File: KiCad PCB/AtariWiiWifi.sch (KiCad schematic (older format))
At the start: 16 parts, among them J1 DB9_Male, J1A1 Conn_01x09, J2 DB9_Male, J2A1 Conn_01x09, U1 PCAL6416APW, U2 AD5242, U3 AD5242, U4 ESP32

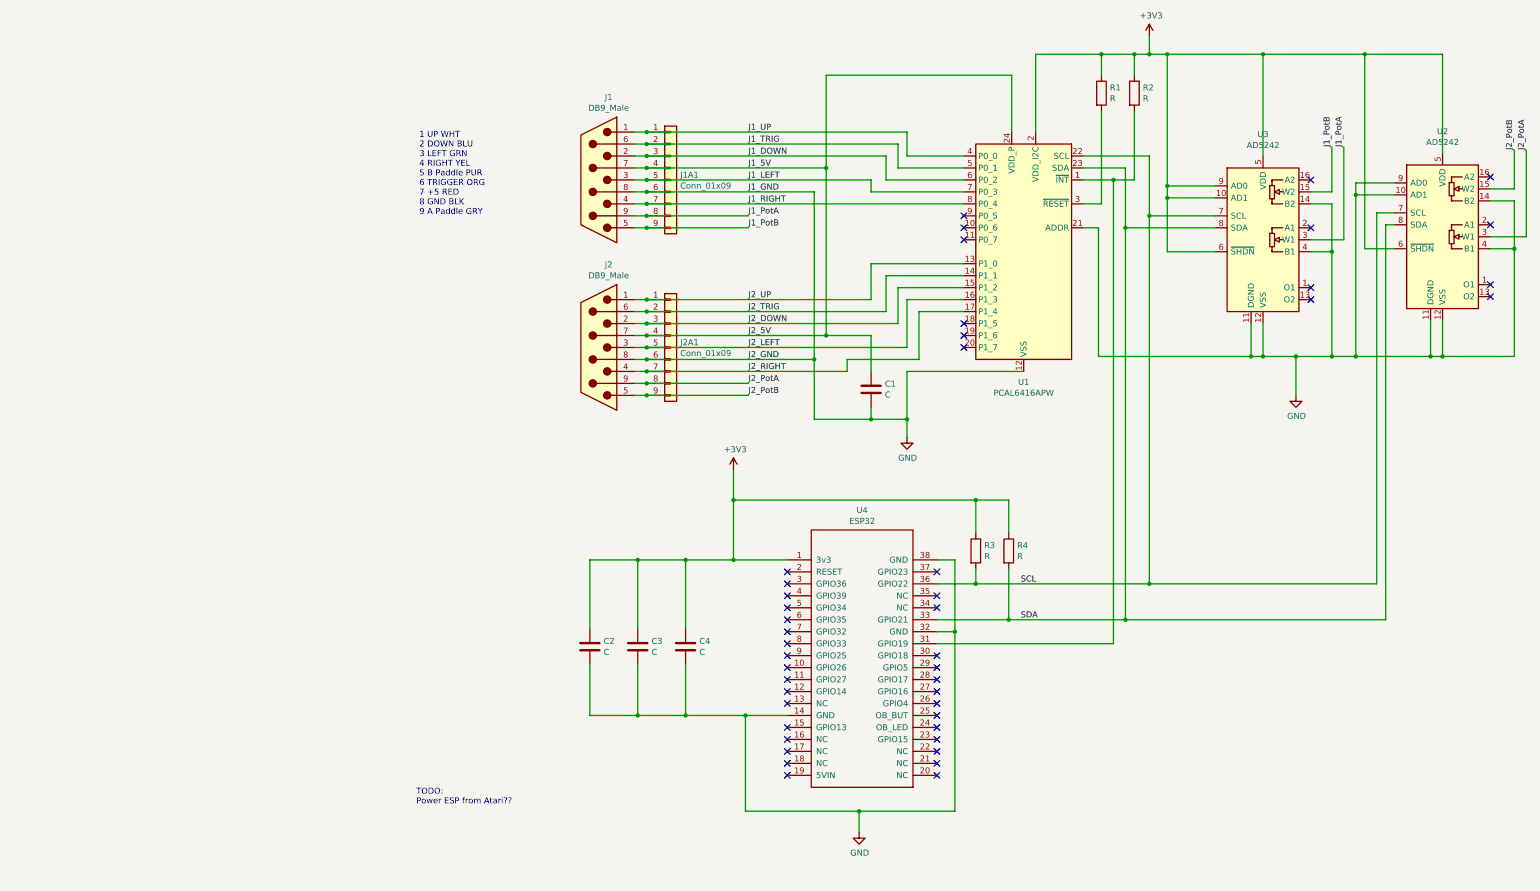
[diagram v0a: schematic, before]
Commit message: Update PCB to Rev 2
Fixed Digital pots connected to ground instead of +5.

Added jumper to power ESP from Atari
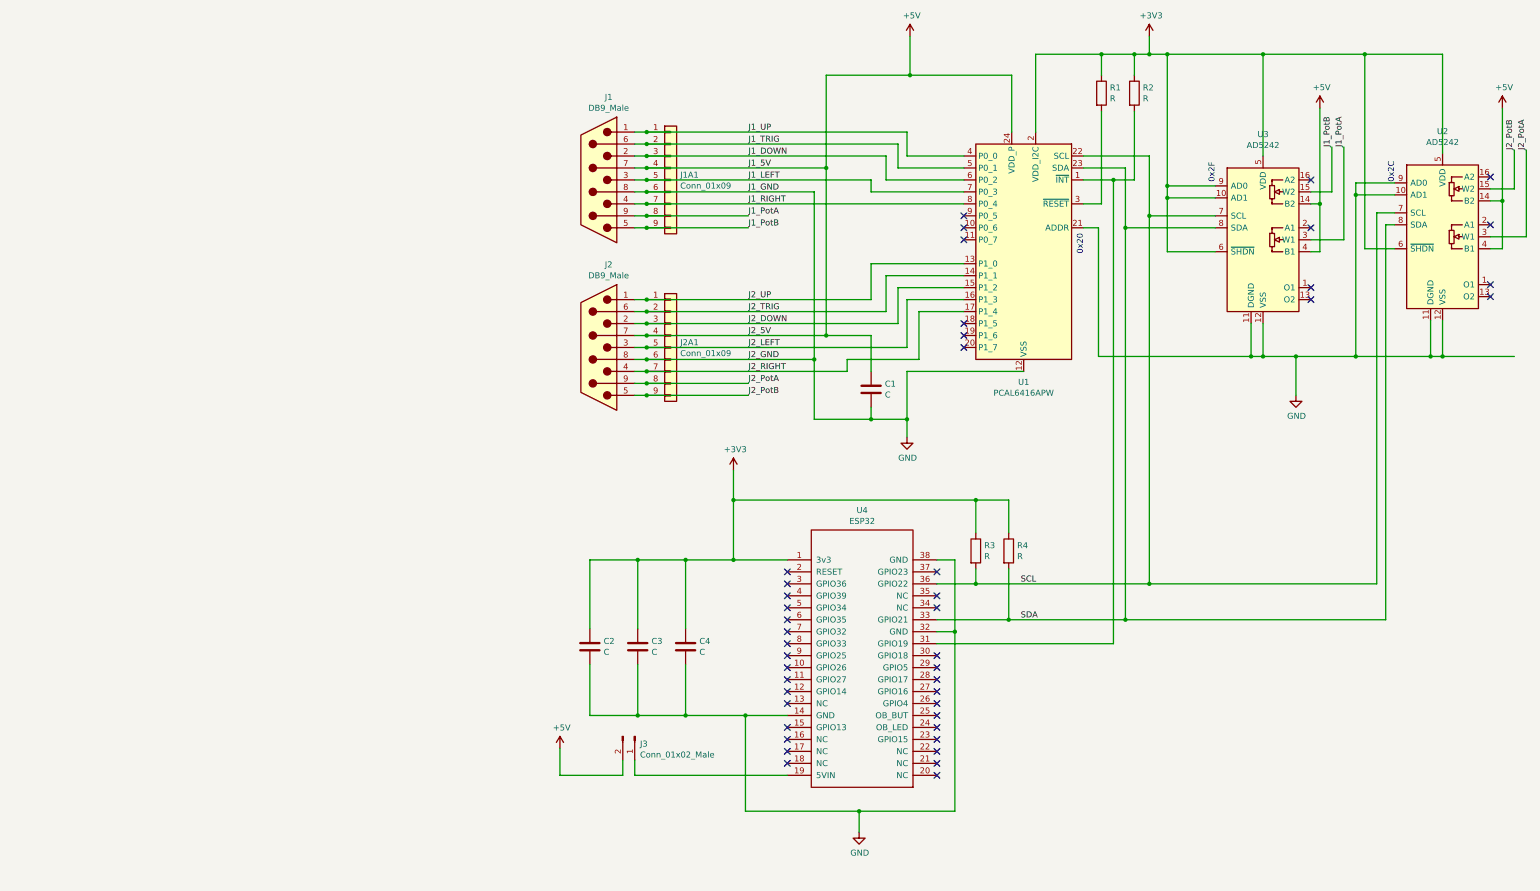
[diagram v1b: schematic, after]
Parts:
- added J3: Conn_01x02_Male, Pin_Headers:Pin_Header_Straight_1x02_Pitch2.54mm, symbol Connector:Conn_01x02_Male
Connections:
- net GND: no longer U2.14 (B2), U2.4 (B1), U3.14 (B2), U3.4 (B1)
- net at U4.19 (5VIN): now also J3.1 (Pin_1)
- net J1_5V renamed +5V
- net +5V: now also U2.14 (B2), U2.4 (B1), U3.14 (B2), U3.4 (B1), J3.2 (Pin_2)
- no-connect marks 45 -> 44
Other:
- note added: "0x20"
- note added: "0x2C"
- note added: "0x2F"
- note removed: "1 UP WHT\n2 DOWN BLU\n3 LEFT GRN\n4 RIGHT YEL\n5 B Paddle PUR\n6 TRIGGER ORG\n7 +5 RED\n8 GND BLK\n9 A Paddle GRY"
- note removed: "TODO:\nPower ESP from Atari??"
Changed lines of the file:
@@
 encoding utf-8
 Sheet 1 1
-Title ""
-Date ""
-Rev ""
-Comp ""
+Title "Atari Wii ESP32 Interfae"
+Date "5/15/21"
+Rev "2"
+Comp "mulcmu"
 Comment1 ""
 Comment2 ""
@@
 	-1   0    0    1
 $EndComp
-Text Notes 1100 2300 0    50   ~ 0
-1 UP WHT\n2 DOWN BLU\n3 LEFT GRN\n4 RIGHT YEL\n5 B Paddle PUR\n6 TRIGGER ORG\n7 +5 RED\n8 GND BLK\n9 A Paddle GRY
 $Comp
 L Connector_Generic:Conn_01x09 J1A1
@@
 $EndComp
 Wire Wire Line
-	4500 1125 6050 1125
+	4500 1125 5200 1125
 Wire Wire Line
 	6050 1125 6050 1600
@@
 Connection ~ 9550 3475
 Wire Wire Line
-	8550 2600 8725 2600
-Wire Wire Line
-	8725 2600 8725 3475
-Connection ~ 8725 3475
-Wire Wire Line
-	8725 3475 8925 3475
-Wire Wire Line
-	8550 2200 8725 2200
-Wire Wire Line
-	8725 2200 8725 2600
-Connection ~ 8725 2600
-Wire Wire Line
-	10050 2575 10250 2575
-Wire Wire Line
-	10250 2575 10250 3475
+	8550 2600 8625 2600
+Wire Wire Line
+	8550 2200 8625 2200
+Wire Wire Line
+	8625 2200 8625 2600
+Wire Wire Line
+	10050 2575 10150 2575
 Wire Wire Line
 	10250 3475 9650 3475
 Connection ~ 9650 3475
 Wire Wire Line
-	10050 2175 10250 2175
-Wire Wire Line
-	10250 2175 10250 2575
-Connection ~ 10250 2575
+	10050 2175 10150 2175
+Wire Wire Line
+	10150 2175 10150 2575
 Text Label 8725 1725 1    50   ~ 0
 J1_PotB
@@
 NoConn ~ 4175 6775
 NoConn ~ 4175 6875
-NoConn ~ 4175 6975
 NoConn ~ 5425 6975
 NoConn ~ 5425 6875
@@
 Connection ~ 8425 3475
 Wire Wire Line
-	8425 3475 8725 3475
-Wire Wire Line
 	9250 2025 8925 2025
 Wire Wire Line
@@
 	4875 3300 4500 3300
 Connection ~ 4500 3300
-Text Notes 1075 7225 0    50   ~ 0
-TODO:\nPower ESP from Atari??
+Text Notes 6650 2625 1    50   ~ 0
+0x20
+Text Notes 7750 2025 1    50   ~ 0
+0x2F
+Text Notes 9250 2025 1    50   ~ 0
+0x2C
+Wire Wire Line
+	8425 3475 8925 3475
+$Comp
+L power:+5V #PWR0106
+U 1 1 60C1B4FC
+P 5200 800
+F 0 "#PWR0106" H 5200 650 50  0001 C CNN
+F 1 "+5V" H 5215 973 50  0000 C CNN
+F 2 "" H 5200 800 50  0001 C CNN
+F 3 "" H 5200 800 50  0001 C CNN
+	1    5200 800
+	1    0    0    -1
+$EndComp
+Wire Wire Line
+	5200 800  5200 1125
+Connection ~ 5200 1125
+Wire Wire Line
+	5200 1125 6050 1125
+$Comp
+L power:+5V #PWR0107
+U 1 1 60C24824
+P 8625 1400
+F 0 "#PWR0107" H 8625 1250 50  0001 C CNN
+F 1 "+5V" H 8640 1573 50  0000 C CNN
+F 2 "" H 8625 1400 50  0001 C CNN
+F 3 "" H 8625 1400 50  0001 C CNN
+	1    8625 1400
+	1    0    0    -1
+$EndComp
+$Comp
+L power:+5V #PWR0108
+U 1 1 60C254AD
+P 10150 1400
+F 0 "#PWR0108" H 10150 1250 50  0001 C CNN
+F 1 "+5V" H 10165 1573 50  0000 C CNN
+F 2 "" H 10150 1400 50  0001 C CNN
+F 3 "" H 10150 1400 50  0001 C CNN
+	1    10150 1400
+	1    0    0    -1
+$EndComp
+Wire Wire Line
+	10150 2175 10150 1400
+Connection ~ 10150 2175
+Wire Wire Line
+	8625 2200 8625 1400
+Connection ~ 8625 2200
+$Comp
+L Connector:Conn_01x02_Male J3
+U 1 1 60C38241
+P 2900 6650
+F 0 "J3" V 2962 6694 50  0000 L CNN
+F 1 "Conn_01x02_Male" V 3053 6694 50  0000 L CNN
+F 2 "Pin_Headers:Pin_Header_Straight_1x02_Pitch2.54mm" H 2900 6650 50  0001 C CNN
+F 3 "~" H 2900 6650 50  0001 C CNN
+	1    2900 6650
+	0    1    1    0
+$EndComp
+Wire Wire Line
+	4175 6975 2900 6975
+Wire Wire Line
+	2900 6975 2900 6850
+Wire Wire Line
+	2800 6850 2800 6975
+Wire Wire Line
+	2800 6975 2275 6975
+Wire Wire Line
+	2275 6975 2275 6750
+$Comp
+L power:+5V #PWR0109
+U 1 1 60C55DB0
+P 2275 6750
+F 0 "#PWR0109" H 2275 6600 50  0001 C CNN
+F 1 "+5V" H 2290 6923 50  0000 C CNN
+F 2 "" H 2275 6750 50  0001 C CNN
+F 3 "" H 2275 6750 50  0001 C CNN
+	1    2275 6750
+	1    0    0    -1
+$EndComp
 $EndSCHEMATC

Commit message: Rev 3 PCB
Update Rev 3 PCB files.
Small Tweak to Schematic for extra bypass cap.
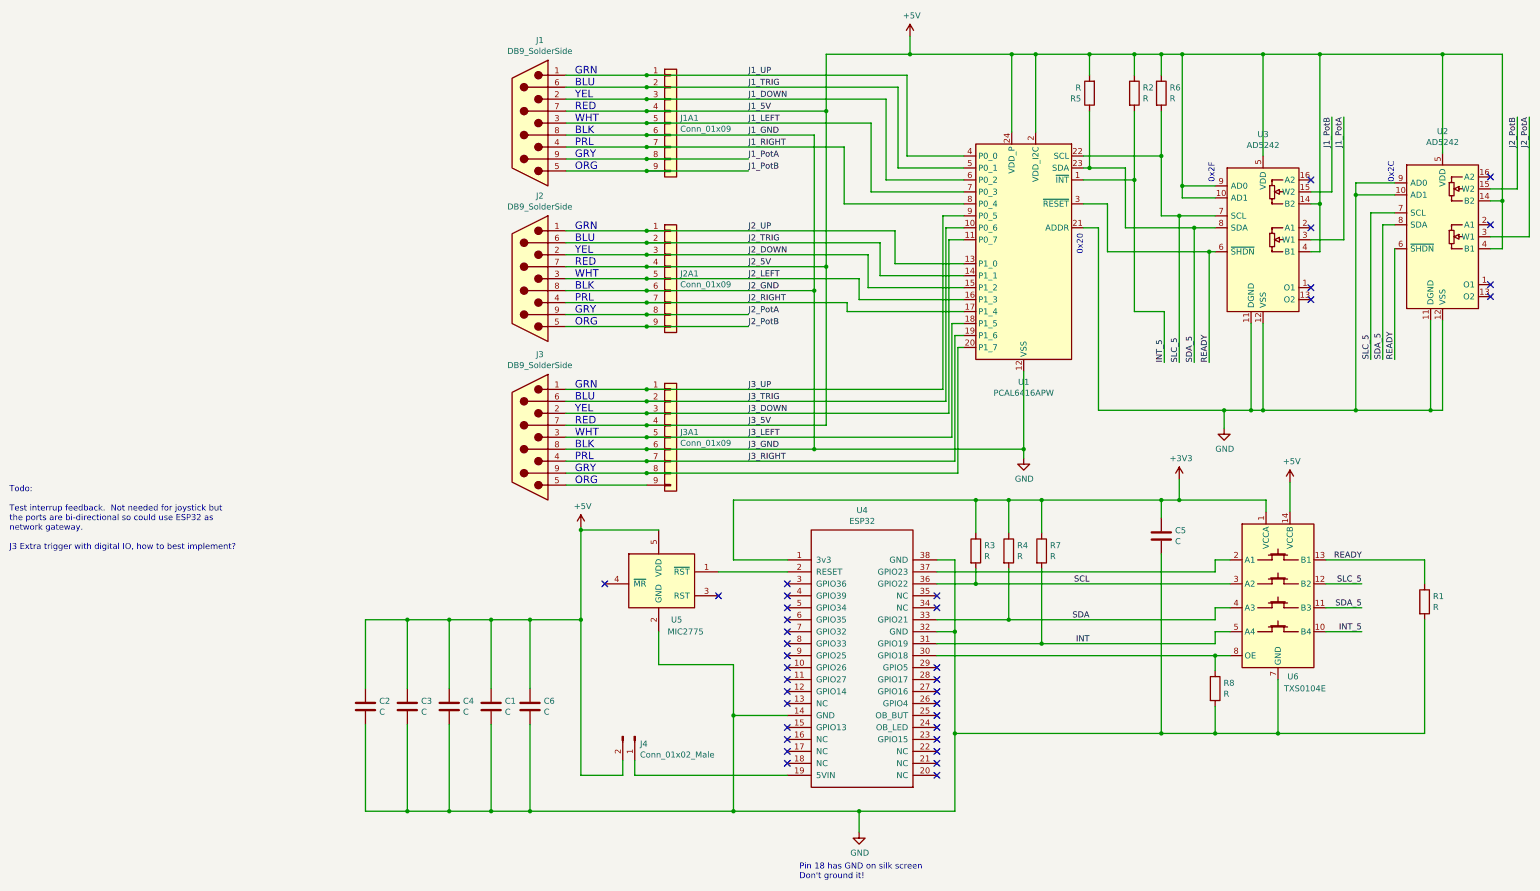
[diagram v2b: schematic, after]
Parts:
- added C5, C6: C, Capacitors_SMD:C_0805_HandSoldering, symbol Device:C
- added J3: DB9_SolderSide, AtariWiiWifi:DSUB-9_Female_Horizontal_P2.77x2.84mm_EdgePinOffset9.90mm_Housed_MountingHolesOffset11.32mm, symbol Connector:DB9_Male
- added J3A1: Conn_01x09, Pin_Headers:Pin_Header_Straight_1x09_Pitch2.54mm, symbol Connector_Generic:Conn_01x09
- added R5, R6, R7, R8: R, Resistors_SMD:R_0805_HandSoldering, symbol Device:R
- added U5: MIC2775, TO_SOT_Packages_SMD:SOT-23-5, symbol AtariWiiWifi:MIC2775
- added U6: TXS0104E, Housings_SSOP:TSSOP-14_4.4x5mm_Pitch0.65mm, symbol AtariWiiWifi:TXS0104E
- J1, J2: value DB9_Male -> DB9_SolderSide
- renumbered J3 to J4
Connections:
- net +3V3: now also C5.1, R7.1, U6.1 (VCCA); no longer C2.1, C3.1, C4.1, R1.1, R2.1, U1.2 (VDD_I2C), U2.5 (VDD), U2.6 (~SHDN), U3.10 (AD1), U3.5 (VDD), U3.6 (~SHDN), U3.9 (AD0)
- net +5V: now also C2.1, C3.1, C4.1, R2.1, U1.2 (VDD_I2C), U2.5 (VDD), U3.10 (AD1), U3.5 (VDD), U3.9 (AD0), C6.1, J3.7, J3A1.4 (Pin_4), R5.2, R6.1, U5.5 (VDD), U6.14 (VCCB)
- net GND: now also R1.2, C5.2, C6.2, J3.8, J3A1.6 (Pin_6), R8.2, U5.2 (GND), U6.7 (GND)
- net SCL: now also U6.3 (A2); no longer U1.22 (SCL), U2.7 (SCL), U3.7 (SCL)
- net SDA: now also U6.4 (A3); no longer U1.23 (SDA), U2.8 (SDA), U3.8 (SDA)
- net INT_5: now reaches R2.2, U1.1 (~INT)
- net INT_5: now also U6.10 (B4); no longer U4.31 (GPIO19)
- net J3_TRIG: now reaches U1.10 (P0_6)
- net J3_TRIG: now also J3.6, J3A1.2 (Pin_2)
- net J3_DOWN: now reaches U1.11 (P0_7)
- net J3_DOWN: now also J3.2, J3A1.3 (Pin_3)
- net J3_LEFT: now reaches U1.18 (P1_5)
- net J3_LEFT: now also J3.3, J3A1.5 (Pin_5)
- net J3_RIGHT: now reaches U1.19 (P1_6)
- net J3_RIGHT: now also J3.4, J3A1.7 (Pin_7)
- net at U1.20 (P1_7): now also J3.9, J3A1.8 (Pin_8)
- net READY: now reaches U1.3 (~RESET)
- net READY: now also R1.1, U2.6 (~SHDN), U3.6 (~SHDN), U6.13 (B1); no longer R1.2
- net J3_UP: now reaches U1.9 (P0_5)
- net J3_UP: now also J3.1, J3A1.1 (Pin_1)
- net at U4.2 (RESET): now also U5.1 (~RST)
- net at U4.30 (GPIO18): now also R8.1, U6.8 (OE)
- net at U4.37 (GPIO23): now also U6.2 (A1)
- new net: J3.5, J3A1.9 (Pin_9)
- new net INT: R7.2, U4.31 (GPIO19), U6.5 (A4)
- new net SDA_5: R5.1, U1.23 (SDA), U2.8 (SDA), U3.8 (SDA), U6.11 (B3)
- new net SLC_5: R6.2, U1.22 (SCL), U2.7 (SCL), U3.7 (SCL), U6.12 (B2)
- no-connect marks 44 -> 37
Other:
- note added: "GRN\nBLU\nYEL\nRED\nWHT\nBLK\nPRL\nGRY\nORG"
- note added: "Pin 18 has GND on silk screen\nDon't ground it!"
- note added: "Todo:\n\nTest interrup feedback. Not needed for joystick but\nthe ports are bi-directional so could use ESP32 as\nnetwork gateway.\n\nJ3 Extra trigger with digital IO, how to best implement?\n"
- moved on the sheet: C1, C2, C3, C4, J1, J1A1, J2, J2A1
